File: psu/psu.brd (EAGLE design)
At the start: 31 x 67 mm, 8 parts

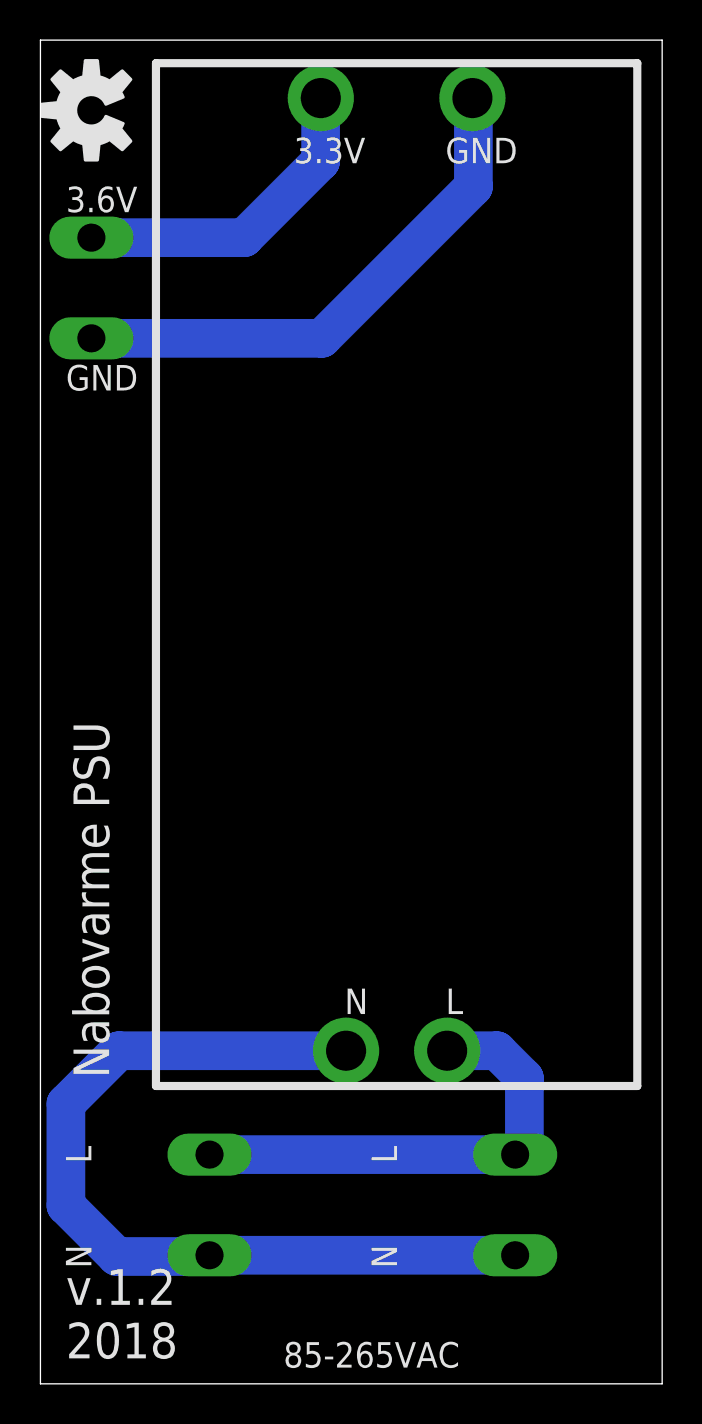
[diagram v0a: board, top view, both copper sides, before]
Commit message: psu pcb: smaller holes for psu module
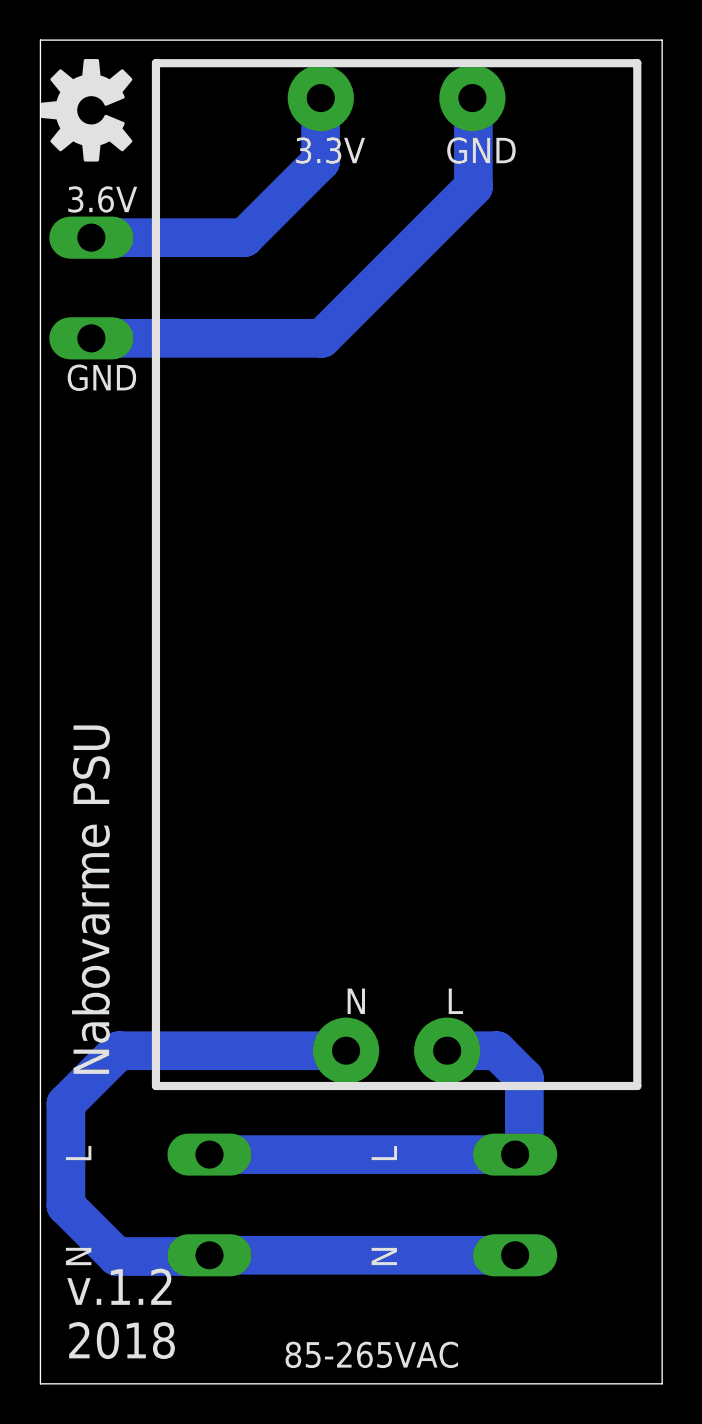
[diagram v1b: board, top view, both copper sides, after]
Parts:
- 3.3V, GND, L, N: value M01PTH_2MM -> (none); device SparkFun (old):1X01_2MM -> 1X01:1X01_1.4MM
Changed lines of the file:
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@@
 <layer number="54" name="bGND_GNDA" color="1" fill="9" visible="no" active="no"/>
 <layer number="56" name="wert" color="7" fill="1" visible="no" active="no"/>
+<layer number="57" name="tCAD" color="7" fill="1" visible="no" active="no"/>
+<layer number="59" name="tCarbon" color="7" fill="1" visible="no" active="no"/>
+<layer number="60" name="bCarbon" color="7" fill="1" visible="no" active="no"/>
 <layer number="90" name="Modules" color="5" fill="1" visible="no" active="no"/>
 <layer number="91" name="Nets" color="2" fill="1" visible="no" active="no"/>
@@
 <layer number="97" name="Info" color="7" fill="1" visible="no" active="no"/>
 <layer number="98" name="Guide" color="6" fill="1" visible="no" active="no"/>
+<layer number="99" name="SpiceOrder" color="7" fill="1" visible="no" active="no"/>
 <layer number="100" name="Muster" color="7" fill="1" visible="no" active="no"/>
 <layer number="101" name="Patch_Top" color="12" fill="4" visible="no" active="yes"/>
@@
 <layer number="106" name="bPlate" color="7" fill="1" visible="no" active="yes"/>
 <layer number="107" name="Crop" color="7" fill="1" visible="no" active="yes"/>
+<layer number="108" name="tplace-old" color="10" fill="1" visible="yes" active="yes"/>
+<layer number="109" name="ref-old" color="11" fill="1" visible="yes" active="yes"/>
+<layer number="110" name="fp0" color="7" fill="1" visible="yes" active="yes"/>
+<layer number="111" name="LPC17xx" color="7" fill="1" visible="yes" active="yes"/>
+<layer number="112" name="tSilk" color="7" fill="1" visible="yes" active="yes"/>
+<layer number="113" name="IDFDebug" color="4" fill="1" visible="yes" active="yes"/>
+<layer number="114" name="Badge_Outline" color="7" fill="1" visible="yes" active="yes"/>
+<layer number="115" name="ReferenceISLANDS" color="7" fill="1" visible="yes" active="yes"/>
 <layer number="116" name="Patch_BOT" color="9" fill="4" visible="no" active="yes"/>
+<layer number="118" name="Rect_Pads" color="7" fill="1" visible="yes" active="yes"/>
 <layer number="121" name="_tsilk" color="7" fill="1" visible="no" active="yes"/>
 <layer number="122" name="_bsilk" color="7" fill="1" visible="no" active="yes"/>
+<layer number="123" name="tTestmark" color="7" fill="1" visible="yes" active="yes"/>
+<layer number="124" name="bTestmark" color="7" fill="1" visible="yes" active="yes"/>
 <layer number="125" name="_tNames" color="7" fill="1" visible="no" active="yes"/>
+<layer number="126" name="_bNames" color="7" fill="1" visible="yes" active="yes"/>
+<layer number="127" name="_tValues" color="7" fill="1" visible="yes" active="yes"/>
+<layer number="128" name="_bValues" color="7" fill="1" visible="yes" active="yes"/>
+<layer number="129" name="Mask" color="7" fill="1" visible="yes" active="yes"/>
+<layer number="131" name="tAdjust" color="7" fill="1" visible="yes" active="yes"/>
+<layer number="132" name="bAdjust" color="7" fill="1" visible="yes" active="yes"/>
 <layer number="144" name="Drill_legend" color="7" fill="1" visible="no" active="yes"/>
+<layer number="150" name="Notes" color="7" fill="1" visible="yes" active="yes"/>
 <layer number="151" name="HeatSink" color="7" fill="1" visible="no" active="yes"/>
+<layer number="152" name="_bDocu" color="7" fill="1" visible="yes" active="yes"/>
+<layer number="153" name="FabDoc1" color="7" fill="1" visible="yes" active="yes"/>
+<layer number="154" name="FabDoc2" color="7" fill="1" visible="yes" active="yes"/>
+<layer number="155" name="FabDoc3" color="7" fill="1" visible="yes" active="yes"/>
 <layer number="199" name="Contour" color="7" fill="1" visible="no" active="yes"/>
 <layer number="200" name="200bmp" color="1" fill="10" visible="no" active="yes"/>
@@
 <layer number="223" name="223bmp" color="24" fill="1" visible="no" active="no"/>
 <layer number="224" name="224bmp" color="25" fill="1" visible="no" active="no"/>
+<layer number="225" name="225bmp" color="7" fill="1" visible="yes" active="yes"/>
+<layer number="226" name="226bmp" color="7" fill="1" visible="yes" active="yes"/>
+<layer number="227" name="227bmp" color="7" fill="1" visible="yes" active="yes"/>
+<layer number="228" name="228bmp" color="7" fill="1" visible="yes" active="yes"/>
+<layer number="229" name="229bmp" color="7" fill="1" visible="yes" active="yes"/>
+<layer number="230" name="230bmp" color="7" fill="1" visible="yes" active="yes"/>
+<layer number="231" name="231bmp" color="7" fill="1" visible="yes" active="yes"/>
+<layer number="232" name="Eagle3D_PG2" color="7" fill="1" visible="yes" active="yes"/>
+<layer number="233" name="Eagle3D_PG3" color="7" fill="1" visible="yes" active="yes"/>
+<layer number="248" name="Housing" color="7" fill="1" visible="yes" active="yes"/>
+<layer number="249" name="Edge" color="7" fill="1" visible="yes" active="yes"/>
 <layer number="250" name="Descript" color="3" fill="1" visible="no" active="no"/>
 <layer number="251" name="SMDround" color="12" fill="11" visible="no" active="no"/>
 <layer number="254" name="cooling" color="7" fill="1" visible="no" active="yes"/>
+<layer number="255" name="routoute" color="7" fill="1" visible="yes" active="yes"/>
 </layers>
 <board>
@@
 </autorouter>
 <elements>
-<element name="N" library="SparkFun (old)" package="1X01_2MM" value="M01PTH_2MM" x="15.24" y="16.61" smashed="yes">
+<element name="N" library="1X01" package="1X01_1.4MM" package3d_urn="urn:adsk.eagle:package:38029/1" value="" x="15.24" y="16.61" smashed="yes">
 <attribute name="NAME" x="15.1638" y="18.4388" size="1.27" layer="25" font="vector"/>
 </element>
-<element name="L" library="SparkFun (old)" package="1X01_2MM" value="M01PTH_2MM" x="20.28" y="16.61" smashed="yes">
+<element name="L" library="1X01" package="1X01_1.4MM" package3d_urn="urn:adsk.eagle:package:38029/1" value="" x="20.28" y="16.61" smashed="yes">
 <attribute name="NAME" x="20.2038" y="18.4388" size="1.27" layer="25" font="vector"/>
 </element>
-<element name="3.3V" library="SparkFun (old)" package="1X01_2MM" value="M01PTH_2MM" x="13.98" y="64.11" smashed="yes">
+<element name="3.3V" library="1X01" package="1X01_1.4MM" package3d_urn="urn:adsk.eagle:package:38029/1" value="" x="13.98" y="64.11" smashed="yes">
 <attribute name="NAME" x="12.6338" y="60.8588" size="1.27" layer="25" font="vector"/>
 </element>
-<element name="GND" library="SparkFun (old)" package="1X01_2MM" value="M01PTH_2MM" x="21.54" y="64.11" smashed="yes">
+<element name="GND" library="1X01" package="1X01_1.4MM" package3d_urn="urn:adsk.eagle:package:38029/1" value="" x="21.54" y="64.11" smashed="yes">
 <attribute name="NAME" x="20.1938" y="60.8588" size="1.27" layer="25" font="vector"/>
 </element>
@@
 which will not be processed correctly with this version.
 </note>
+<note version="8.3" severity="warning">
+Since Version 8.3, EAGLE supports URNs for individual library
+assets (packages, symbols, and devices). The URNs of those assets
+will not be understood (or retained) with this version.
+</note>
+<note version="8.3" severity="warning">
+Since Version 8.3, EAGLE supports the association of 3D packages
+with devices in libraries, schematics, and board files. Those 3D
+packages will not be understood (or retained) with this version.
+</note>
 </compatibility>
